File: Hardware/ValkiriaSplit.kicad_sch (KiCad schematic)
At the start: 0 parts

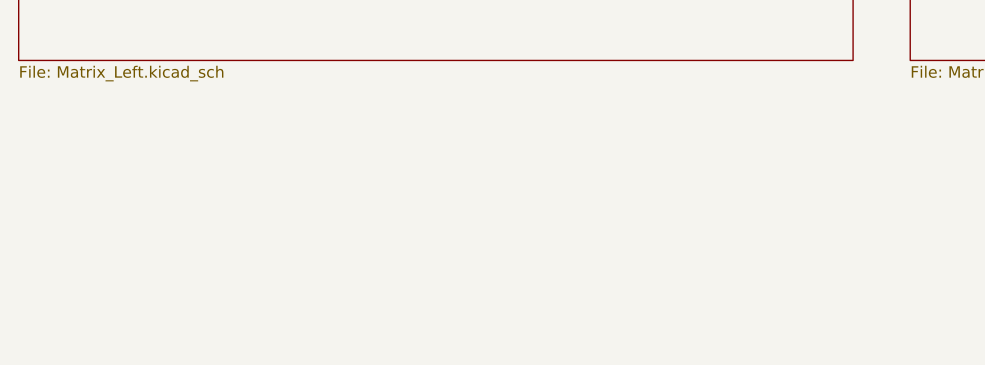
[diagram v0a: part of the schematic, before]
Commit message: Layout coordination
Coordinated the layout with the schematic.
Finished the initial switch layout.
Need to decide on a complete layout for the keyboard and assign the auxiliary keys.
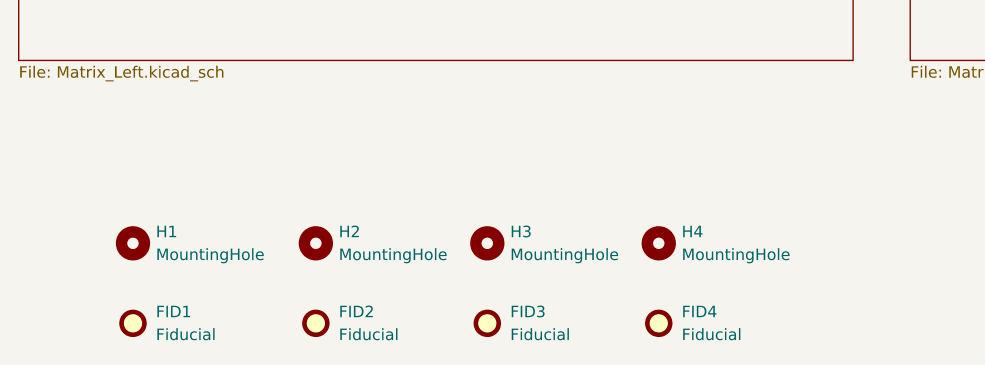
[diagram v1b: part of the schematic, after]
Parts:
- added FID1, FID2, FID3, FID4: Fiducial, Fiducial:Fiducial_1mm_Mask2mm, symbol Mechanical:Fiducial
- added H1, H2, H3, H4: MountingHole, MountingHole:ToolingHole_1.152mm, symbol Mechanical:MountingHole

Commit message: Board outline and routing
Enlarged the board outline by 0.5mm for proper fitment of the switch receptacles.
Updated the footprint for the switch receptacles.
Changed the JTAG connector for a custom one.
Need to review the size of the PCB area dedicated to the MCU and the screen.
Need to consider removing the additional reset button.
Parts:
- H1, H2, H3, H4: value MountingHole -> Tooling
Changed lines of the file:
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@@
 			)
 		)
-		(property "Value" "MountingHole"
+		(property "Value" "Tooling"
 			(at 107.95 170.1799 0)
 			(show_name no)
@@
 			)
 		)
-		(property "Value" "MountingHole"
+		(property "Value" "Tooling"
 			(at 88.9 170.1799 0)
 			(show_name no)
@@
 			)
 		)
-		(property "Value" "MountingHole"
+		(property "Value" "Tooling"
 			(at 68.58 170.1799 0)
 			(show_name no)
@@
 			)
 		)
-		(property "Value" "MountingHole"
+		(property "Value" "Tooling"
 			(at 127 170.1799 0)
 			(show_name no)
